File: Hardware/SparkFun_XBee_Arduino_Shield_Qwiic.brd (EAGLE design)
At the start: 53.3 x 59.7 mm, 167 parts, among them J4 QWIIC_RIGHT_ANGLE, Q1 220mA/50V/3.5Ω, Q3 3.1A/30V/105mΩ, Q5 20V/4.2A/52mΩ/1.4W, U1 FSUSB42MUX, U2 AP63203, U3 ESD Diode, U4 FT231XS, U5 ESD Diode, X1 JUMPER-SMT_2_NO_SILK

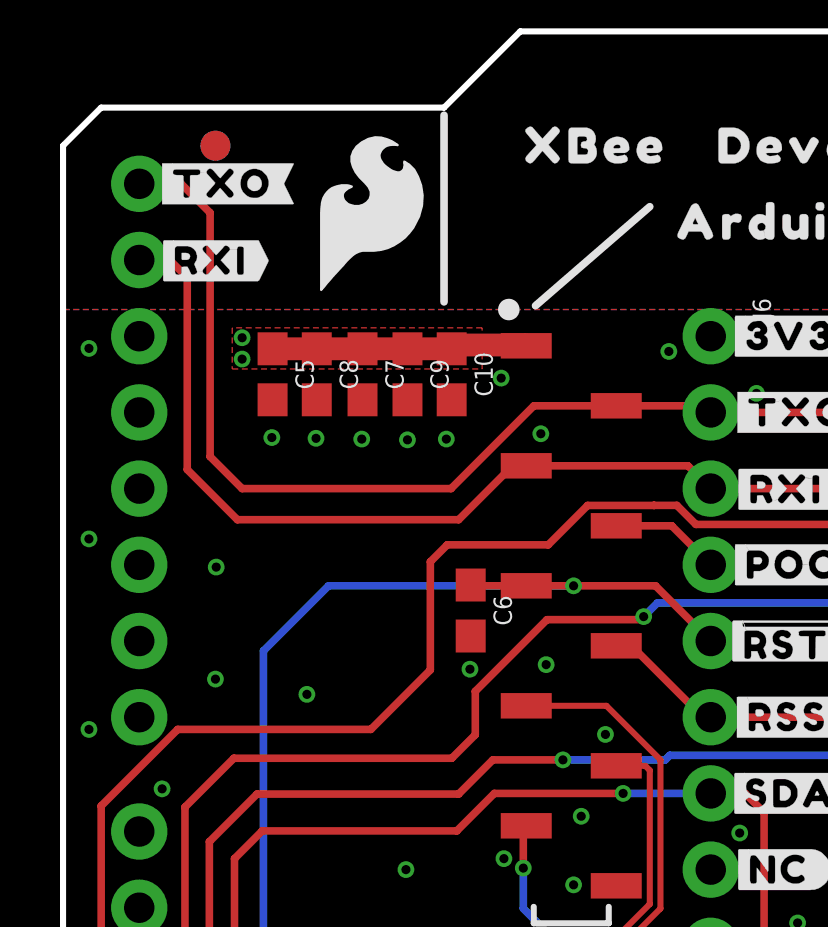
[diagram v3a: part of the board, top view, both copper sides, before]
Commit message: Adds switch to UART lines for disconnect
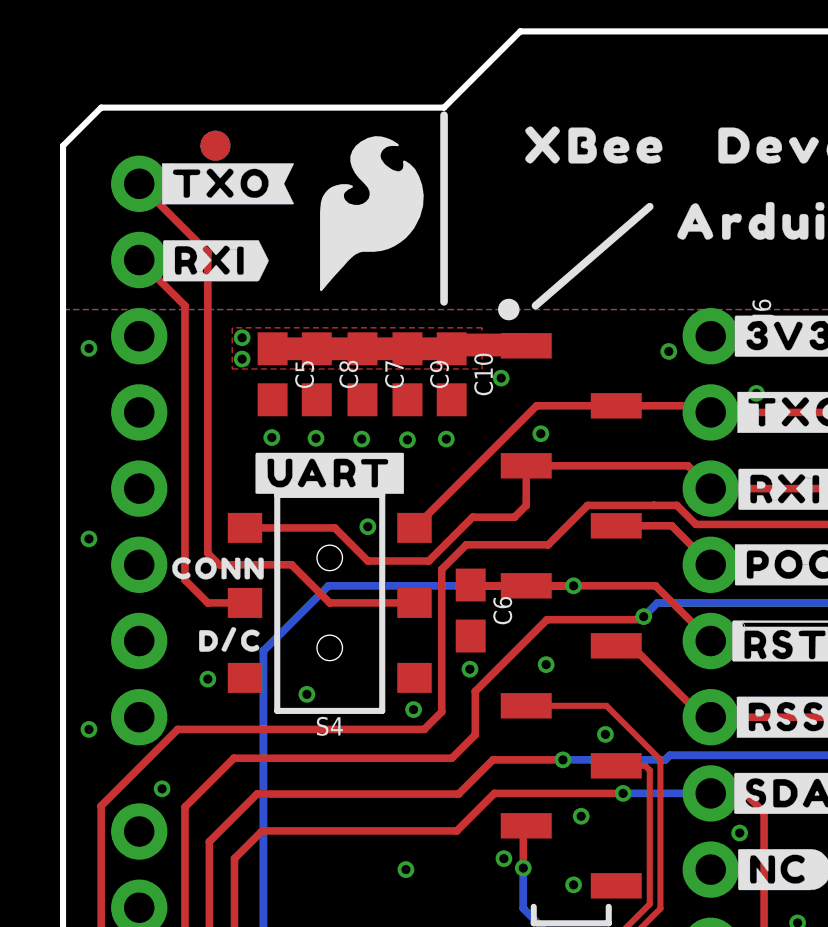
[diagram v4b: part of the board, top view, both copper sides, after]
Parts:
- added S4: (no value), SparkFun-Switches:SWITCH_DPDT_SMD_AYZ0202
- added U$91: (no value), top:#UART#4048234
- added U$92: (no value), top:CONN4048235
- added U$95: (no value), top:D#C4048236
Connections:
- new net D13/TXO-R3: B1.RX, S4.5
- new net D14/RXI-R3: B1.TX, S4.2
- net D13/TXO: now also S4.6; no longer B1.RX
- net D14/RXI: now also S4.3; no longer B1.TX
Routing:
- net D13/TXO-R3: track 0.00 -> 20.8 mm
- net D13/TXO: track 69.1 -> 51.5 mm
- net D14/RXI-R3: track 0.00 -> 13.6 mm
- net D14/RXI: track 73.6 -> 64.5 mm
- net D1/SCL: track 94.7 -> 95.4 mm
- net GND: vias 117 -> 118
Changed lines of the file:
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@@
 <setting verticaltext="up"/>
 </settings>
-<grid distance="0.05" unitdist="inch" unit="inch" style="dots" multiple="1" display="yes" altdistance="0.001" altunitdist="inch" altunit="inch"/>
+<grid distance="0.05" unitdist="inch" unit="inch" style="dots" multiple="1" display="yes" altdistance="0.005" altunitdist="inch" altunit="inch"/>
 <layers>
 <layer number="1" name="Top" color="4" fill="1" visible="yes" active="yes"/>
-<layer number="2" name="Route2" color="23" fill="1" visible="yes" active="yes"/>
-<layer number="15" name="Route15" color="39" fill="1" visible="yes" active="yes"/>
+<layer number="2" name="Route2" color="23" fill="1" visible="no" active="yes"/>
+<layer number="15" name="Route15" color="39" fill="1" visible="no" active="yes"/>
 <layer number="16" name="Bottom" color="3" fill="1" visible="yes" active="yes"/>
 <layer number="17" name="Pads" color="26" fill="1" visible="yes" active="yes"/>
@@
 <layer number="37" name="tTest" color="7" fill="1" visible="no" active="yes"/>
 <layer number="38" name="bTest" color="7" fill="1" visible="no" active="yes"/>
-<layer number="39" name="tKeepout" color="4" fill="11" visible="yes" active="yes"/>
+<layer number="39" name="tKeepout" color="4" fill="11" visible="no" active="yes"/>
 <layer number="40" name="bKeepout" color="1" fill="11" visible="no" active="yes"/>
 <layer number="41" name="tRestrict" color="4" fill="10" visible="no" active="yes"/>
@@
 <attribute name="VALUE" x="17.78" y="20.32" size="0.6096" layer="27" font="vector" ratio="20" rot="R180" align="bottom-center"/>
 </element>
+<element name="S4" library="SparkFun-Switches" package="SWITCH_DPDT_SMD_AYZ0202" value="" x="8.89" y="40.64" smashed="yes" rot="R90">
+<attribute name="NAME" x="8.89" y="36.83" size="0.6096" layer="25" font="vector" ratio="20" rot="R180" align="bottom-center"/>
+<attribute name="PROD_ID" value="SWCH-08179" x="8.89" y="40.64" size="1.778" layer="27" font="vector" ratio="15" rot="R90" display="off"/>
+<attribute name="SF_SKU" value="COM-00597" x="8.89" y="40.64" size="1.778" layer="27" font="vector" ratio="15" rot="R90" display="off"/>
+<attribute name="VALUE" x="8.89" y="44.45" size="0.6096" layer="27" font="vector" ratio="20" rot="R180" align="top-center"/>
+</element>
+<element name="U$91" library="top" package="#UART#4048234" value="" x="8.89" y="44.958" smashed="yes"/>
+<element name="U$92" library="top" package="CONN4048235" value="" x="5.207" y="41.783" smashed="yes"/>
+<element name="U$95" library="top" package="D#C4048236" value="" x="5.588" y="39.37" smashed="yes"/>
 </elements>
 <signals>
@@
 <wire x1="13.2588" y1="3.2512" x2="10.60954375" y2="3.2512" width="0.254" layer="1"/>
 <wire x1="2.54" y1="10.16" x2="1.27" y2="11.43" width="0.254" layer="1"/>
-<wire x1="12.2428" y1="38.4048" x2="12.2428" y2="42.0116" width="0.254" layer="1"/>
-<wire x1="12.2428" y1="42.0116" x2="12.807" y2="42.5758" width="0.254" layer="1"/>
+<wire x1="12.6238" y1="37.0078" x2="12.6238" y2="41.7576" width="0.254" layer="1"/>
+<wire x1="12.6238" y1="41.7576" x2="13.442" y2="42.5758" width="0.254" layer="1"/>
 <wire x1="17.4847875" y1="43.889" x2="19.7000125" y2="43.889" width="0.254" layer="1"/>
 <wire x1="19.7000125" y1="43.889" x2="19.6978125" y2="43.8912" width="0.254" layer="1"/>
-<wire x1="12.807" y1="42.5758" x2="16.1715875" y2="42.5758" width="0.254" layer="1"/>
+<wire x1="13.442" y1="42.5758" x2="16.1715875" y2="42.5758" width="0.254" layer="1"/>
 <wire x1="16.1715875" y1="42.5758" x2="17.4847875" y2="43.889" width="0.254" layer="1"/>
 <wire x1="20.46050625" y1="43.8912" x2="21.09550625" y2="43.2562" width="0.254" layer="1"/>
 <wire x1="1.27" y1="11.43" x2="1.27" y2="33.87170625" width="0.254" layer="1"/>
 <wire x1="1.27" y1="33.87170625" x2="3.82189375" y2="36.4236" width="0.254" layer="1"/>
-<wire x1="3.82189375" y1="36.4236" x2="10.2616" y2="36.4236" width="0.254" layer="1"/>
-<wire x1="10.2616" y1="36.4236" x2="12.2428" y2="38.4048" width="0.254" layer="1"/>
+<wire x1="3.82189375" y1="36.4236" x2="12.0396" y2="36.4236" width="0.254" layer="1"/>
+<wire x1="12.0396" y1="36.4236" x2="12.6238" y2="37.0078" width="0.254" layer="1"/>
 <wire x1="19.6978125" y1="43.8912" x2="20.46050625" y2="43.8912" width="0.254" layer="1"/>
 <wire x1="30.505403125" y1="43.2562" x2="30.5308" y2="43.2816" width="0.254" layer="1"/>
@@
 <via x="48.2854" y="41.8338" extent="1-16" drill="0.3048"/>
 <via x="48.2854" y="46.9138" extent="1-16" drill="0.3048"/>
-<via x="5.1054" y="41.8338" extent="1-16" drill="0.3048"/>
-<via x="5.08" y="38.1" extent="1-16" drill="0.3048"/>
+<via x="4.826" y="38.1" extent="1-16" drill="0.3048"/>
 <via x="11.43" y="31.75" extent="1-16" drill="0.3048"/>
 <via x="8.89" y="12.7" extent="1-16" drill="0.3048"/>
@@
 <via x="11.8872" y="11.049" extent="1-16" drill="0.3048"/>
 <via x="15.1384" y="8.1788" extent="1-16" drill="0.3048"/>
+<via x="10.16" y="43.18" extent="1-16" drill="0.3048"/>
+<via x="11.684" y="37.084" extent="1-16" drill="0.3048"/>
 </signal>
 <signal name="3.3V">
@@
 <wire x1="21.37" y1="47.21" x2="21.59" y2="46.99" width="0.254" layer="1"/>
 <contactref element="U4" pad="4"/>
-<wire x1="12.93401875" y1="44.45" x2="15.69401875" y2="47.21" width="0.254" layer="1"/>
-<wire x1="15.69401875" y1="47.21" x2="18.44" y2="47.21" width="0.254" layer="1"/>
 <wire x1="37.7825" y1="21.48920625" x2="32.6898" y2="26.58190625" width="0.254" layer="1"/>
 <wire x1="37.7825" y1="19.1897" x2="37.7825" y2="21.48920625" width="0.254" layer="1"/>
 <wire x1="32.6898" y1="26.58190625" x2="32.6898" y2="45.0088" width="0.254" layer="1"/>
 <wire x1="32.6898" y1="45.0088" x2="30.7086" y2="46.99" width="0.254" layer="1"/>
-<contactref element="B1" pad="RX"/>
-<wire x1="4.9022" y1="53.6448" x2="3.937" y2="54.61" width="0.254" layer="1"/>
-<wire x1="3.937" y1="54.61" x2="2.54" y2="54.61" width="0.254" layer="1"/>
-<wire x1="4.9022" y1="53.6448" x2="4.9022" y2="45.5168" width="0.254" layer="1"/>
-<wire x1="5.969" y1="44.45" x2="12.93401875" y2="44.45" width="0.254" layer="1"/>
-<wire x1="4.9022" y1="45.5168" x2="5.969" y2="44.45" width="0.254" layer="1"/>
+<contactref element="S4" pad="6"/>
+<wire x1="15.785" y1="47.21" x2="18.44" y2="47.21" width="0.254" layer="1"/>
+<wire x1="11.715" y1="43.14" x2="15.785" y2="47.21" width="0.254" layer="1"/>
 </signal>
 <signal name="D14/RXI">
@@
 <wire x1="20.83" y1="45.21" x2="15.44" y2="45.21" width="0.254" layer="1"/>
 <contactref element="U4" pad="20"/>
-<wire x1="14.984" y1="45.21" x2="15.44" y2="45.21" width="0.254" layer="1"/>
-<wire x1="14.984" y1="45.21" x2="13.188" y2="43.414" width="0.254" layer="1"/>
 <wire x1="39.6875" y1="13.8303" x2="39.6875" y2="15.5575" width="0.254" layer="1"/>
 <wire x1="34.6456" y1="16.9164" x2="33.5026" y2="18.0594" width="0.254" layer="1"/>
@@
 <wire x1="31.5722" y1="29.9212" x2="31.5722" y2="43.8658" width="0.254" layer="1"/>
 <wire x1="30.988" y1="44.45" x2="21.59" y2="44.45" width="0.254" layer="1"/>
-<contactref element="B1" pad="TX"/>
-<wire x1="4.1402" y1="45.085" x2="4.1402" y2="51.4858" width="0.254" layer="1"/>
-<wire x1="4.1402" y1="51.4858" x2="3.556" y2="52.07" width="0.254" layer="1"/>
-<wire x1="3.556" y1="52.07" x2="2.54" y2="52.07" width="0.254" layer="1"/>
-<wire x1="5.8112" y1="43.414" x2="4.1402" y2="45.085" width="0.254" layer="1"/>
-<wire x1="13.188" y1="43.414" x2="5.8112" y2="43.414" width="0.254" layer="1"/>
+<contactref element="S4" pad="3"/>
+<wire x1="6.065" y1="43.14" x2="9.057" y2="43.14" width="0.254" layer="1"/>
+<wire x1="9.057" y1="43.14" x2="10.16" y2="42.037" width="0.254" layer="1"/>
+<wire x1="10.16" y1="42.037" x2="12.192" y2="42.037" width="0.254" layer="1"/>
+<wire x1="12.192" y1="42.037" x2="13.6525" y2="43.4975" width="0.254" layer="1"/>
+<wire x1="13.6525" y1="43.4975" x2="15.0495" y2="43.4975" width="0.254" layer="1"/>
+<wire x1="15.44" y1="43.888" x2="15.44" y2="45.21" width="0.254" layer="1"/>
+<wire x1="15.0495" y1="43.4975" x2="15.44" y2="43.888" width="0.254" layer="1"/>
 </signal>
 <signal name="D12/SPI_POCI">
@@
 </polygon>
 </signal>
+<signal name="D13/TXO-R3">
+<contactref element="B1" pad="RX"/>
+<contactref element="S4" pad="5"/>
+<wire x1="4.826" y1="52.324" x2="2.54" y2="54.61" width="0.254" layer="1"/>
+<wire x1="11.715" y1="40.64" x2="8.89" y2="40.64" width="0.254" layer="1"/>
+<wire x1="8.89" y1="40.64" x2="7.62" y2="41.91" width="0.254" layer="1"/>
+<wire x1="5.207" y1="41.91" x2="7.62" y2="41.91" width="0.254" layer="1"/>
+<wire x1="4.826" y1="52.324" x2="4.826" y2="42.291" width="0.254" layer="1"/>
+<wire x1="4.826" y1="42.291" x2="5.207" y2="41.91" width="0.254" layer="1"/>
+</signal>
+<signal name="D14/RXI-R3">
+<contactref element="B1" pad="TX"/>
+<contactref element="S4" pad="2"/>
+<wire x1="6.065" y1="40.64" x2="4.826" y2="40.64" width="0.254" layer="1"/>
+<wire x1="4.064" y1="50.546" x2="2.54" y2="52.07" width="0.254" layer="1"/>
+<wire x1="4.826" y1="40.64" x2="4.064" y2="41.402" width="0.254" layer="1"/>
+<wire x1="4.064" y1="41.402" x2="4.064" y2="50.546" width="0.254" layer="1"/>
+</signal>
 </signals>

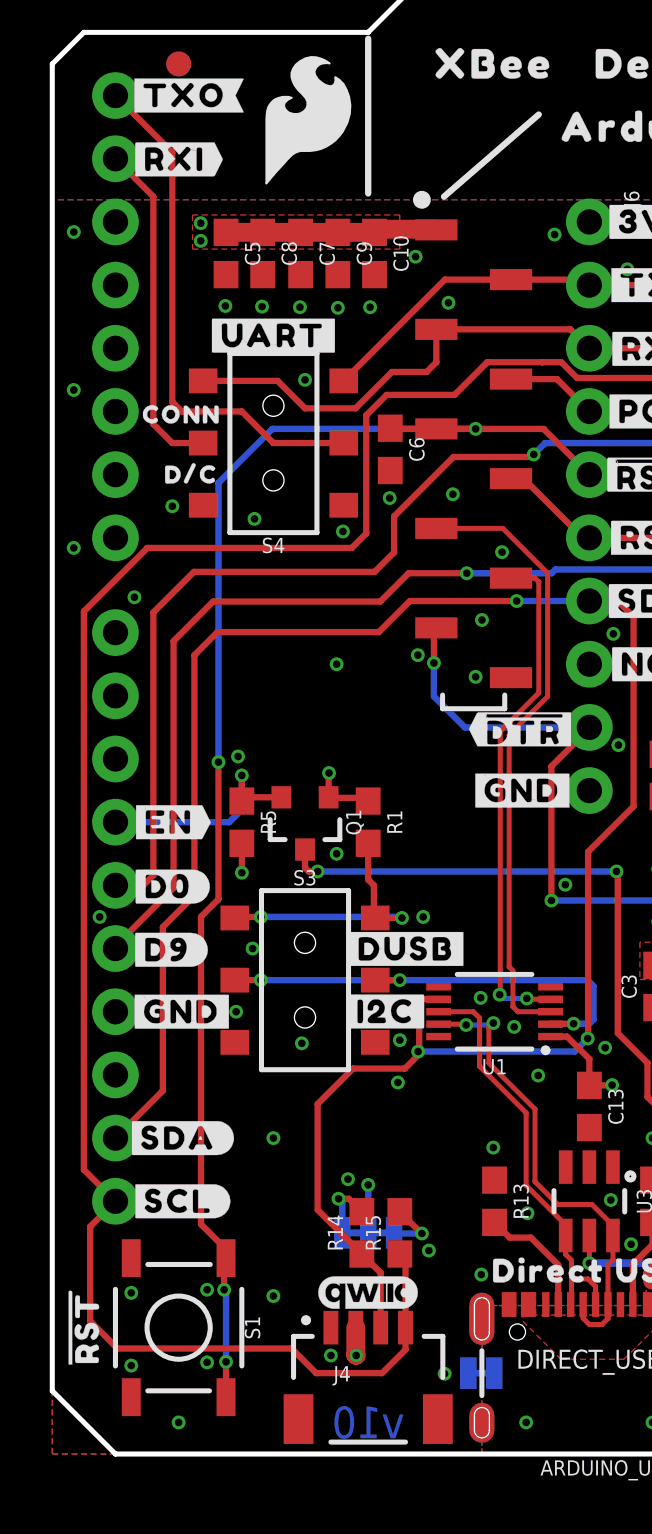
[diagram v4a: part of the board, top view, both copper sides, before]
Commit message: Changes silk on switch and increments the version number
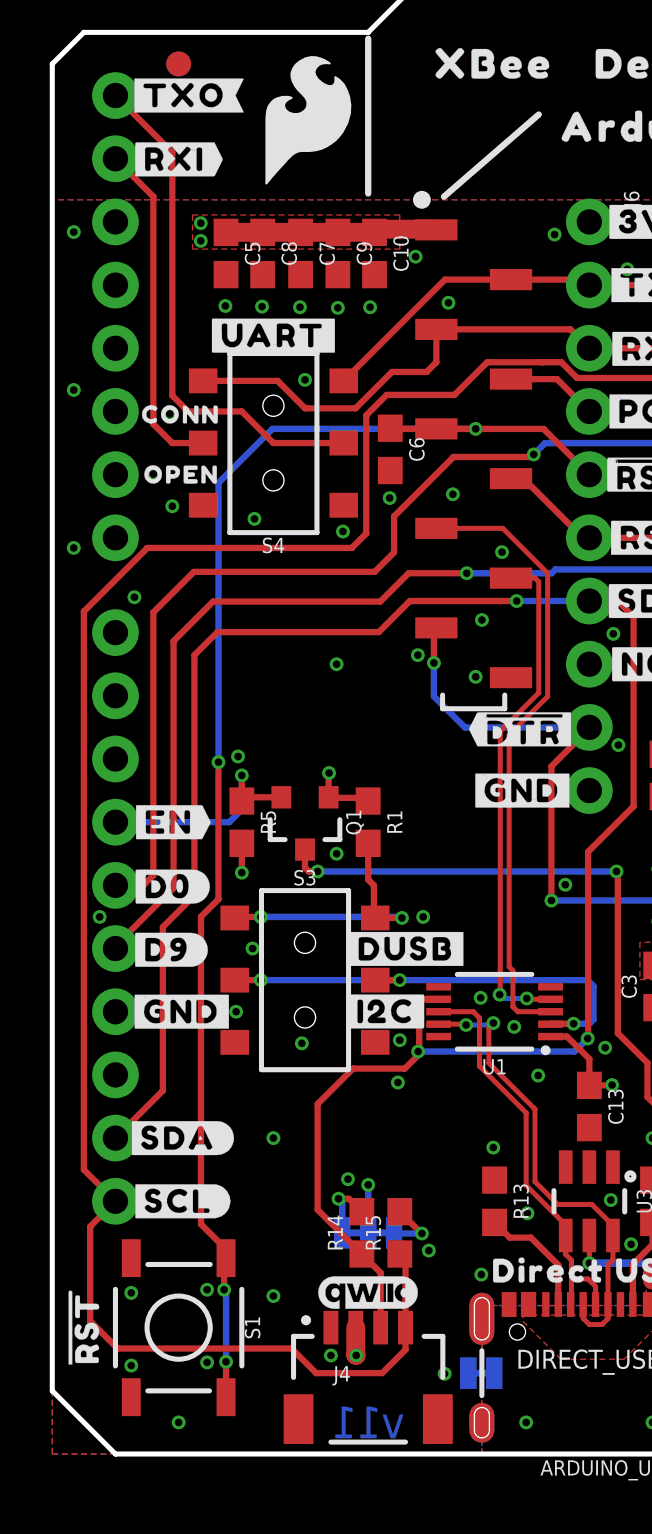
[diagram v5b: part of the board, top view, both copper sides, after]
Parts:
- U$95: device top:D#C4048236 -> top:OPEN4048238
- moved U$95 0.38 mm to (5.20, 39.4)
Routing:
- net GND: vias 118 -> 120
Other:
- board text added: "Four Layer Board 1 oz Outer Layer 0.5 oz Inner Layer JLC7628 Stackup Lead-Free HASL 1.6mm Thickness Red Soldermask White Silkscreen Material: TG135-140"
- board text added: "v11"
- board text removed: "1.6mm Thickness"
- board text removed: "1oz Outer Layer 0.5oz Inner Layer JLC0416H-7628 Stackup"
- board text removed: "Four Layer Board"
- board text removed: "Lead Free HASL"
- board text removed: "Material: FR4: TG135-140"
- board text removed: "Red Soldermask"
- board text removed: "White Silk"
- board text removed: "v10"
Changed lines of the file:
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@@
 <setting verticaltext="up"/>
 </settings>
-<grid distance="0.05" unitdist="inch" unit="inch" style="dots" multiple="1" display="yes" altdistance="0.005" altunitdist="inch" altunit="inch"/>
+<grid distance="0.05" unitdist="inch" unit="inch" style="dots" multiple="1" display="yes" altdistance="0.001" altunitdist="inch" altunit="inch"/>
 <layers>
 <layer number="1" name="Top" color="4" fill="1" visible="yes" active="yes"/>
@@
 <wire x1="0" y1="55.88" x2="0" y2="2.54" width="0.2032" layer="20"/>
 <text x="17.78" y="-36.83" size="1.778" layer="51" font="vector">Elias Santistevan</text>
-<text x="12.7" y="1.27" size="1.27" layer="16" font="vector" ratio="15" rot="MR0" align="center">v10</text>
+<text x="12.7" y="1.27" size="1.27" layer="16" font="vector" ratio="15" rot="MR0" align="center">v11</text>
 <wire x1="2.54" y1="0" x2="50.8" y2="0" width="0.2032" layer="20"/>
 <wire x1="53.34" y1="2.54" x2="53.34" y2="57.15" width="0.2032" layer="20"/>
@@
 <text x="47.703" y="48.207" size="1.778" layer="15" font="vector" ratio="15">3</text>
 <text x="49.227" y="48.207" size="1.778" layer="16" font="vector" ratio="15" rot="SMR0">4</text>
-<text x="78.74" y="44.45" size="1.778" layer="51" font="vector" ratio="15">Four Layer Board</text>
-<text x="78.74" y="26.67" size="1.778" layer="51" font="vector" ratio="15">1.6mm Thickness</text>
-<text x="78.74" y="30.48" size="1.778" layer="51" font="vector" ratio="15">Lead Free HASL</text>
-<text x="78.74" y="34.29" size="1.778" layer="51" font="vector" ratio="15">1oz Outer Layer
-0.5oz Inner Layer
-JLC0416H-7628 Stackup</text>
+<text x="78.74" y="22.86" size="1.778" layer="51" font="vector">Four Layer Board
+1 oz Outer Layer
+0.5 oz Inner Layer
+JLC7628 Stackup
+Lead-Free HASL
+1.6mm Thickness
+Red Soldermask
+White Silkscreen
+Material: TG135-140</text>
 <dimension x1="45.72" y1="24.13" x2="0" y2="24.13" x3="22.86" y3="-24.13" textsize="1.778" textratio="15" layer="47" unit="inch"/>
 <dimension x1="45.72" y1="24.13" x2="53.34" y2="24.13" x3="49.53" y3="-24.13" textsize="1.778" textratio="15" layer="47" unit="inch"/>
@@
 <dimension x1="50.8" y1="19.05" x2="50.8" y2="36.83" x3="60.96" y3="27.94" textsize="1.778" textratio="15" layer="47" unit="inch"/>
 <dimension x1="15.24" y1="59.69" x2="11.43" y2="57.15" x3="-3.81" y3="58.42" textsize="1.778" textratio="15" layer="47" dtype="vertical" unit="inch"/>
-<text x="78.74" y="22.86" size="1.778" layer="51" font="vector" ratio="15">Red Soldermask</text>
-<text x="78.74" y="19.05" size="1.778" layer="51" font="vector" ratio="15">White Silk</text>
-<text x="78.74" y="15.24" size="1.778" layer="51" font="vector" ratio="15">Material: FR4: TG135-140</text>
 </plain>
 <attributes>
@@
 </element>
 <element name="U$91" library="top" package="#UART#4048234" value="" x="8.89" y="44.958" smashed="yes"/>
-<element name="U$92" library="top" package="CONN4048235" value="" x="5.207" y="41.783" smashed="yes"/>
-<element name="U$95" library="top" package="D#C4048236" value="" x="5.588" y="39.37" smashed="yes"/>
+<element name="U$92" library="top" package="CONN4048235" value="" x="5.1735" y="41.783" smashed="yes"/>
+<element name="U$95" library="top" package="OPEN4048238" value="" x="5.2039" y="39.37" smashed="yes"/>
 </elements>
 <signals>
@@
 <via x="10.16" y="43.18" extent="1-16" drill="0.3048"/>
 <via x="11.684" y="37.084" extent="1-16" drill="0.3048"/>
+<via x="4.7244" y="41.8084" extent="1-16" drill="0.3048"/>
+<via x="4.064" y="39.3954" extent="1-16" drill="0.3048"/>
 </signal>
 <signal name="3.3V">
@@
 <wire x1="11.715" y1="40.64" x2="8.89" y2="40.64" width="0.254" layer="1"/>
 <wire x1="8.89" y1="40.64" x2="7.62" y2="41.91" width="0.254" layer="1"/>
-<wire x1="5.207" y1="41.91" x2="7.62" y2="41.91" width="0.254" layer="1"/>
-<wire x1="4.826" y1="52.324" x2="4.826" y2="42.291" width="0.254" layer="1"/>
-<wire x1="4.826" y1="42.291" x2="5.207" y2="41.91" width="0.254" layer="1"/>
+<wire x1="5.461" y1="41.91" x2="7.62" y2="41.91" width="0.254" layer="1"/>
+<wire x1="4.826" y1="52.324" x2="4.826" y2="42.545" width="0.254" layer="1"/>
+<wire x1="4.826" y1="42.545" x2="5.461" y2="41.91" width="0.254" layer="1"/>
 </signal>
 <signal name="D14/RXI-R3">
